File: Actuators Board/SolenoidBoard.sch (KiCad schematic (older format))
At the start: 31 parts, among them J10 Conn_01x02_Male, J9 Conn_01x02_Male, Q1 MMDT2222A

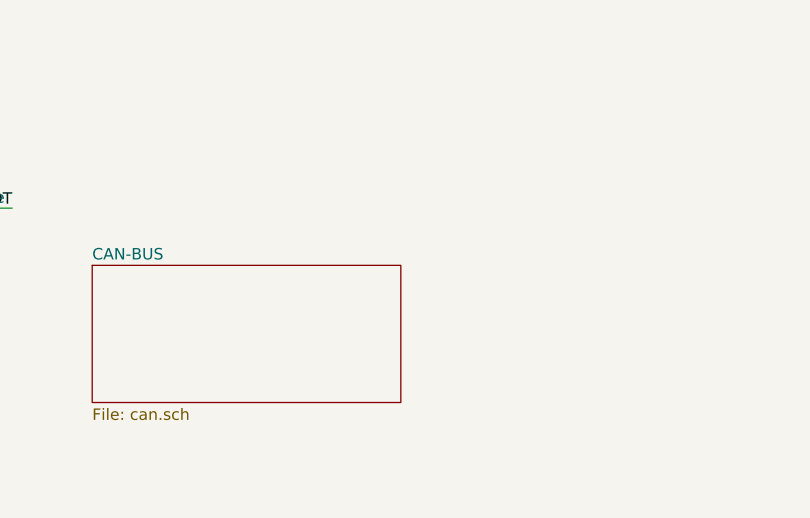
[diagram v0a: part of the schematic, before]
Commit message: Place Hierarchical Pins from CAN sheet to each board.
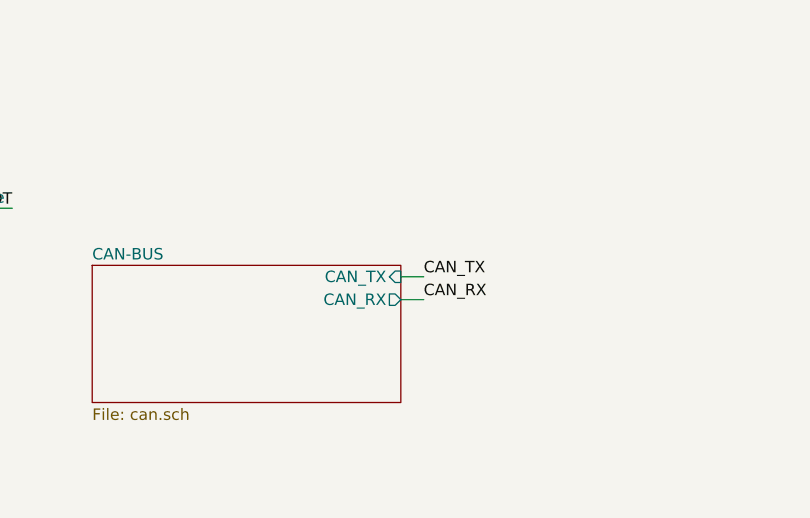
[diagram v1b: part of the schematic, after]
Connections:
- wire segments 78 -> 80
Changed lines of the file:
@@
 F0 "CAN-BUS" 50
 F1 "can.sch" 50
+F2 "CAN_TX" I R 4600 6800 50
+F3 "CAN_RX" O R 4600 6900 50
 $EndSheet
 Text Label 5000 2150 0    50   ~ 0
@@
 Wire Wire Line
 	9600 1350 9750 1350
+Wire Wire Line
+	4600 6800 4700 6800
+Wire Wire Line
+	4600 6900 4700 6900
+Text Label 4700 6800 0    50   ~ 0
+CAN_TX
+Text Label 4700 6900 0    50   ~ 0
+CAN_RX
 $EndSCHEMATC

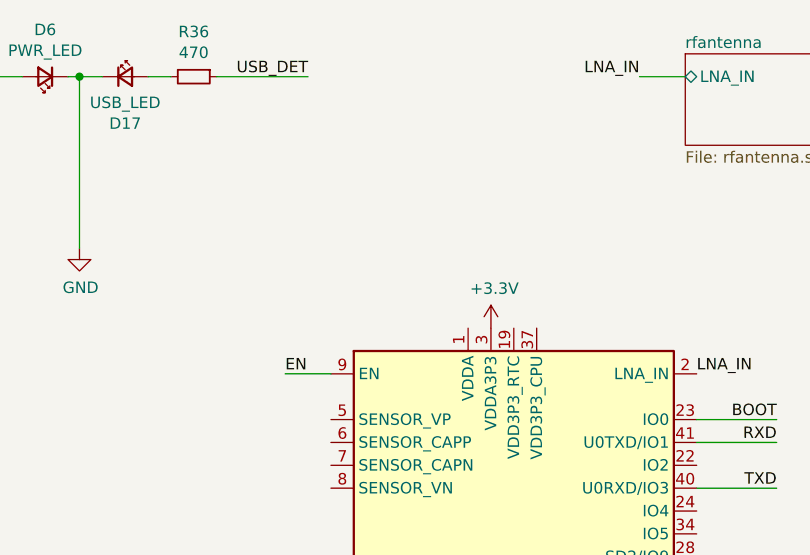
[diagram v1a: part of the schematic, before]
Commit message: Connected 3.3V to ESP32 according to schematic
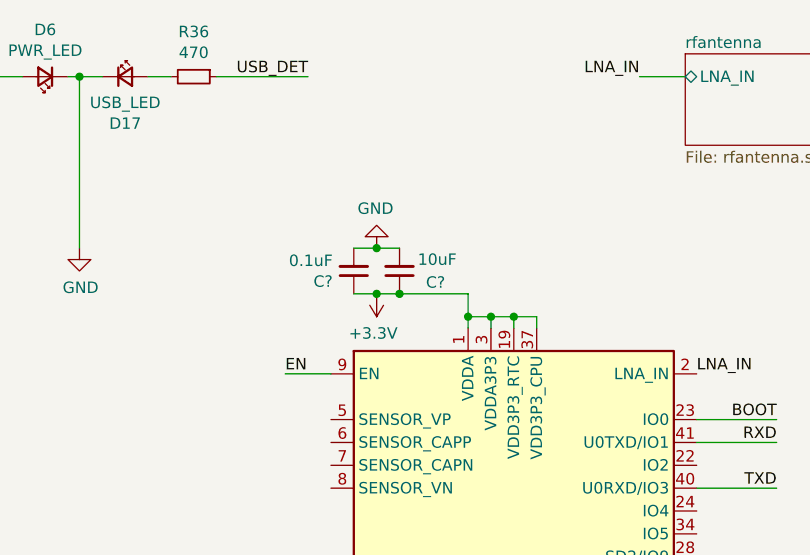
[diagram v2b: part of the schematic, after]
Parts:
- added C?: 10uF, symbol Device:C_Small
- added C?: 0.1uF, symbol Device:C_Small
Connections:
- wire segments 80 -> 93
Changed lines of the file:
@@
 $EndDescr
-$Comp
-L power:+3.3V #PWR020
-U 1 1 5DA60792
-P 4100 1950
-F 0 "#PWR020" H 4100 1800 50  0001 C CNN
-F 1 "+3.3V" H 4115 2123 50  0000 C CNN
-F 2 "" H 4100 1950 50  0001 C CNN
-F 3 "" H 4100 1950 50  0001 C CNN
-	1    4100 1950
-	1    0    0    -1
-$EndComp
 $Comp
 L power:GND #PWR021
@@
 Text Label 4700 6900 0    50   ~ 0
 CAN_RX
+$Comp
+L power:+3.3V #PWR?
+U 1 1 61AA6780
+P 3600 1800
+AR Path="/61AA6780" Ref="#PWR?"  Part="1"
+AR Path="/61AA560B/61AA6780" Ref="#PWR?"  Part="1"
+F 0 "#PWR?" H 3600 1650 50  0001 C CNN
+F 1 "+3.3V" H 3615 1973 50  0000 C CNN
+F 2 "" H 3600 1800 50  0001 C CNN
+F 3 "" H 3600 1800 50  0001 C CNN
+	1    3600 1800
+	-1   0    0    1
+$EndComp
+$Comp
+L Device:C_Small C?
+U 1 1 61AA6786
+P 3700 1700
+AR Path="/61AA6786" Ref="C?"  Part="1"
+AR Path="/61AA560B/61AA6786" Ref="C?"  Part="1"
+F 0 "C?" H 3500 1750 50  0000 L CNN
+F 1 "10uF" H 3450 1650 50  0000 L CNN
+F 2 "" H 3700 1700 50  0001 C CNN
+F 3 "~" H 3700 1700 50  0001 C CNN
+	1    3700 1700
+	-1   0    0    1
+$EndComp
+$Comp
+L Device:C_Small C?
+U 1 1 61AA678C
+P 3500 1700
+AR Path="/61AA678C" Ref="C?"  Part="1"
+AR Path="/61AA560B/61AA678C" Ref="C?"  Part="1"
+F 0 "C?" H 3592 1746 50  0000 L CNN
+F 1 "0.1uF" H 3592 1655 50  0000 L CNN
+F 2 "" H 3500 1700 50  0001 C CNN
+F 3 "~" H 3500 1700 50  0001 C CNN
+	1    3500 1700
+	-1   0    0    1
+$EndComp
+Wire Wire Line
+	3700 1800 3600 1800
+Wire Wire Line
+	3700 1600 3600 1600
+$Comp
+L power:GND #PWR?
+U 1 1 61AA6794
+P 3600 1600
+AR Path="/61AA6794" Ref="#PWR?"  Part="1"
+AR Path="/61AA560B/61AA6794" Ref="#PWR?"  Part="1"
+F 0 "#PWR?" H 3600 1350 50  0001 C CNN
+F 1 "GND" H 3605 1427 50  0000 C CNN
+F 2 "" H 3600 1600 50  0001 C CNN
+F 3 "" H 3600 1600 50  0001 C CNN
+	1    3600 1600
+	-1   0    0    1
+$EndComp
+Connection ~ 3600 1600
+Wire Wire Line
+	3600 1600 3500 1600
+Connection ~ 3600 1800
+Wire Wire Line
+	3600 1800 3500 1800
+Wire Wire Line
+	4000 1900 4100 1900
+Wire Wire Line
+	4100 1900 4100 1950
+Wire Wire Line
+	4000 1900 4000 1950
+Wire Wire Line
+	4100 1900 4200 1900
+Wire Wire Line
+	4200 1900 4200 1950
+Connection ~ 4100 1900
+Wire Wire Line
+	4200 1900 4300 1900
+Wire Wire Line
+	4300 1900 4300 1950
+Connection ~ 4200 1900
+Wire Wire Line
+	3700 1800 4000 1800
+Wire Wire Line
+	4000 1800 4000 1900
+Connection ~ 3700 1800
+Connection ~ 4000 1900
 $EndSCHEMATC

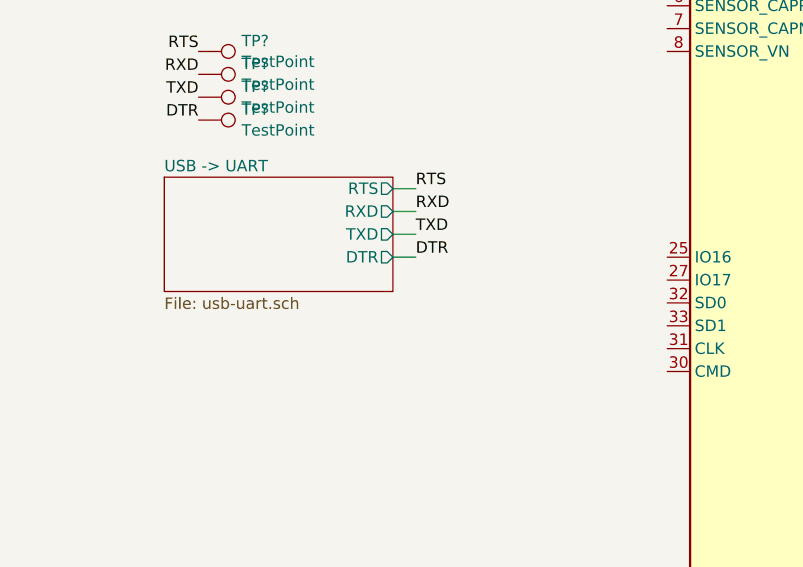
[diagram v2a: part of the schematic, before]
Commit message: Connected 3.3V output from USB-UART converter
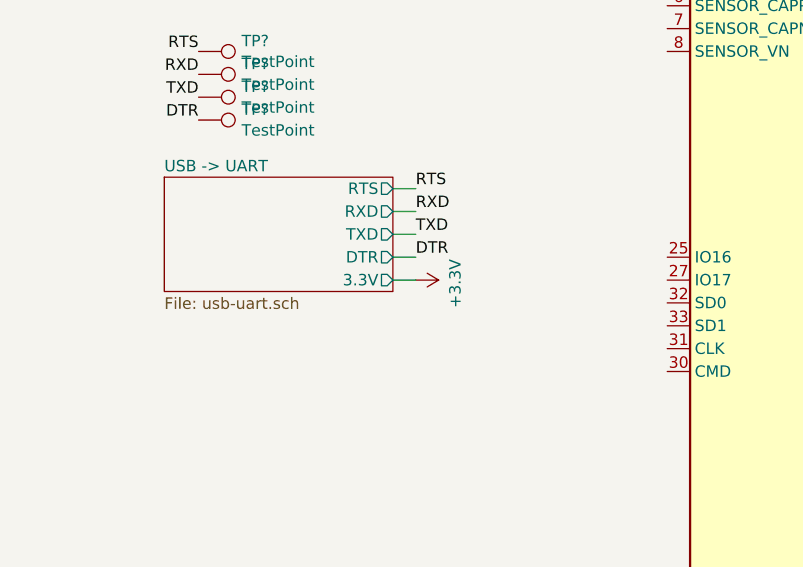
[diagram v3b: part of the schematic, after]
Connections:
- wire segments 93 -> 94
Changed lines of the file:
@@
 F4 "TXD" O R 2200 3450 50
 F5 "DTR" O R 2200 3550 50
+F6 "3.3V" O R 2200 3650 50
 $EndSheet
 $Comp
@@
 Connection ~ 3700 1800
 Connection ~ 4000 1900
+Wire Wire Line
+	2200 3650 2300 3650
+$Comp
+L power:+3.3V #PWR?
+U 1 1 61A6DFD2
+P 2300 3650
+AR Path="/61A6DFD2" Ref="#PWR?"  Part="1"
+AR Path="/61AA560B/61A6DFD2" Ref="#PWR?"  Part="1"
+F 0 "#PWR?" H 2300 3500 50  0001 C CNN
+F 1 "+3.3V" H 2315 3823 50  0000 C CNN
+F 2 "" H 2300 3650 50  0001 C CNN
+F 3 "" H 2300 3650 50  0001 C CNN
+	1    2300 3650
+	0    1    1    0
+$EndComp
 $EndSCHEMATC

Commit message: Swapped IRF620 mosfet with SIJA74DP-T1-GE3
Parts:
- removed Q?: IRF620PBF-BE3, symbol iclr:IRF620PBF-BE3
- added U?: SIJA74DP-T1-GE3, SOT_4DP-T1-GE3_VIS, symbol iclr:SIJA74DP-T1-GE3
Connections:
- wire segments 94 -> 97
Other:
- moved on the sheet: R?
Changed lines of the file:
@@
 LNA_IN
-$Comp
-L iclr:IRF620PBF-BE3 Q?
-U 1 1 61A26E34
-P 9850 2300
-F 0 "Q?" H 9948 2346 50  0000 L CNN
-F 1 "IRF620PBF-BE3" H 9948 2255 50  0000 L CNN
-F 2 "" H 9850 2300 50  0001 C CNN
-F 3 "" H 9850 2300 50  0001 L BNN
-	1    9850 2300
-	1    0    0    -1
-$EndComp
 $Comp
 L Device:D D?
@@
 	1    0    0    -1
 $EndComp
-Text Label 9600 2400 2    50   ~ 0
+Text Label 9450 2450 2    50   ~ 0
 SolEN
 Text Label 5000 3150 0    50   ~ 0
@@
 L power:GND #PWR?
 U 1 1 61A29C79
-P 9850 2650
-F 0 "#PWR?" H 9850 2400 50  0001 C CNN
-F 1 "GND" H 9855 2477 50  0000 C CNN
-F 2 "" H 9850 2650 50  0001 C CNN
-F 3 "" H 9850 2650 50  0001 C CNN
-	1    9850 2650
-	1    0    0    -1
-$EndComp
-Text Label 9850 2100 1    50   ~ 0
+P 9800 2750
+F 0 "#PWR?" H 9800 2500 50  0001 C CNN
+F 1 "GND" H 9805 2577 50  0000 C CNN
+F 2 "" H 9800 2750 50  0001 C CNN
+F 3 "" H 9800 2750 50  0001 C CNN
+	1    9800 2750
+	1    0    0    -1
+$EndComp
+Text Label 9800 2150 1    50   ~ 0
 SolGND
 $Comp
@@
 L Device:R_Small R?
 U 1 1 61A5320F
-P 9600 2550
-F 0 "R?" H 9450 2600 50  0000 L CNN
-F 1 "110" H 9400 2500 50  0000 L CNN
-F 2 "" H 9600 2550 50  0001 C CNN
-F 3 "~" H 9600 2550 50  0001 C CNN
-	1    9600 2550
-	1    0    0    -1
-$EndComp
-Wire Wire Line
-	9600 2450 9600 2400
-Wire Wire Line
-	9600 2400 9650 2400
-Wire Wire Line
-	9600 2650 9850 2650
-Wire Wire Line
-	9850 2650 9850 2500
-Connection ~ 9850 2650
+P 9450 2600
+F 0 "R?" H 9300 2650 50  0000 L CNN
+F 1 "110" H 9250 2550 50  0000 L CNN
+F 2 "" H 9450 2600 50  0001 C CNN
+F 3 "~" H 9450 2600 50  0001 C CNN
+	1    9450 2600
+	1    0    0    -1
+$EndComp
+Wire Wire Line
+	9450 2500 9450 2450
+Wire Wire Line
+	9450 2450 9500 2450
 $Comp
 L Connector:Conn_01x02_Female J?
@@
 	0    1    1    0
 $EndComp
+$Comp
+L iclr:SIJA74DP-T1-GE3 U?
+U 1 1 61AB9D88
+P 9500 2450
+F 0 "U?" H 10100 2550 60  0000 L CNN
+F 1 "SIJA74DP-T1-GE3" H 9962 2447 60  0000 L CNN
+F 2 "SOT_4DP-T1-GE3_VIS" H 9950 2290 60  0001 C CNN
+F 3 "" H 9500 2450 60  0000 C CNN
+	1    9500 2450
+	1    0    0    -1
+$EndComp
+Wire Wire Line
+	9900 2650 9800 2650
+Connection ~ 9800 2650
+Wire Wire Line
+	9800 2650 9700 2650
+Wire Wire Line
+	9450 2700 9450 2750
+Wire Wire Line
+	9450 2750 9800 2750
+Wire Wire Line
+	9800 2750 9800 2650
+Connection ~ 9800 2750
 $EndSCHEMATC

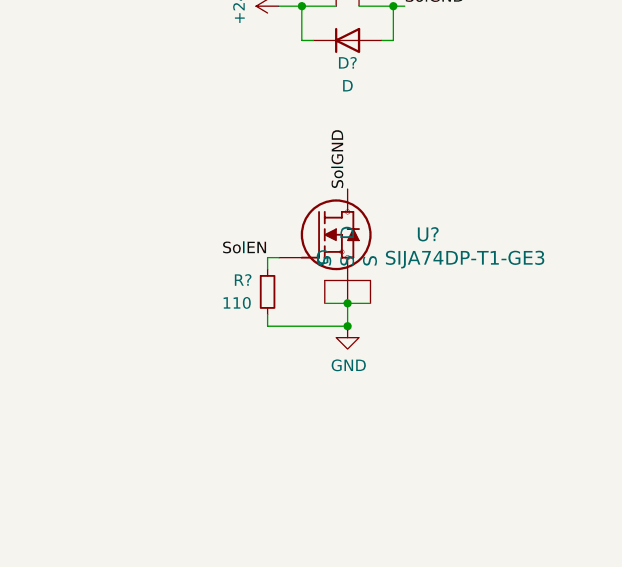
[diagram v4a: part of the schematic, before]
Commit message: Hopefully swapped the mosfet for the last time
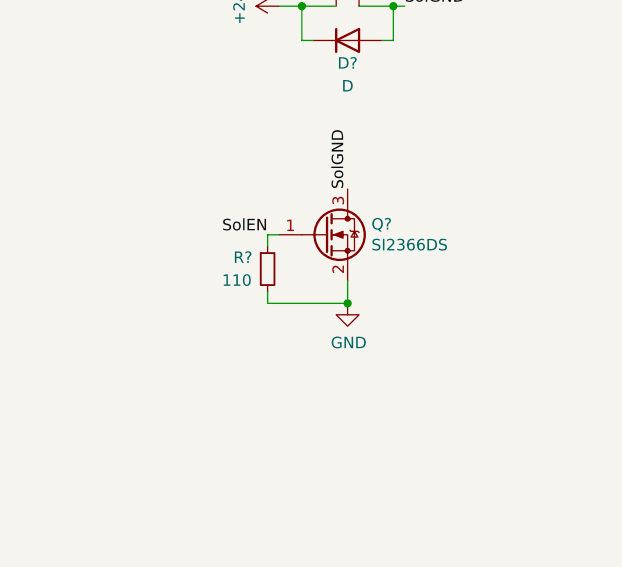
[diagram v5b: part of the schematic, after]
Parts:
- removed U?: SIJA74DP-T1-GE3, SOT_4DP-T1-GE3_VIS, symbol iclr:SIJA74DP-T1-GE3
- added Q?: SI2366DS, Package_TO_SOT_SMD:SOT-23, symbol Transistor_FET:DMN3404L
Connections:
- net GND: now also Q?.2 (S)
- net SolEN: now also Q?.1 (G)
- net SolGND: now also Q?.3 (D)
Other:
- moved on the sheet: R?
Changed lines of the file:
@@
 	1    0    0    -1
 $EndComp
-Text Label 9450 2450 2    50   ~ 0
+Text Label 9450 2350 2    50   ~ 0
 SolEN
 Text Label 5000 3150 0    50   ~ 0
 SolEN
-$Comp
-L power:GND #PWR?
-U 1 1 61A29C79
-P 9800 2750
-F 0 "#PWR?" H 9800 2500 50  0001 C CNN
-F 1 "GND" H 9805 2577 50  0000 C CNN
-F 2 "" H 9800 2750 50  0001 C CNN
-F 3 "" H 9800 2750 50  0001 C CNN
-	1    9800 2750
-	1    0    0    -1
-$EndComp
 Text Label 9800 2150 1    50   ~ 0
 SolGND
@@
 L Device:R_Small R?
 U 1 1 61A5320F
-P 9450 2600
-F 0 "R?" H 9300 2650 50  0000 L CNN
-F 1 "110" H 9250 2550 50  0000 L CNN
-F 2 "" H 9450 2600 50  0001 C CNN
-F 3 "~" H 9450 2600 50  0001 C CNN
-	1    9450 2600
-	1    0    0    -1
-$EndComp
-Wire Wire Line
-	9450 2500 9450 2450
-Wire Wire Line
-	9450 2450 9500 2450
+P 9450 2500
+F 0 "R?" H 9300 2550 50  0000 L CNN
+F 1 "110" H 9250 2450 50  0000 L CNN
+F 2 "" H 9450 2500 50  0001 C CNN
+F 3 "~" H 9450 2500 50  0001 C CNN
+	1    9450 2500
+	1    0    0    -1
+$EndComp
+Wire Wire Line
+	9450 2400 9450 2350
+Wire Wire Line
+	9450 2350 9500 2350
 $Comp
 L Connector:Conn_01x02_Female J?
@@
 	0    1    1    0
 $EndComp
-$Comp
-L iclr:SIJA74DP-T1-GE3 U?
-U 1 1 61AB9D88
-P 9500 2450
-F 0 "U?" H 10100 2550 60  0000 L CNN
-F 1 "SIJA74DP-T1-GE3" H 9962 2447 60  0000 L CNN
-F 2 "SOT_4DP-T1-GE3_VIS" H 9950 2290 60  0001 C CNN
-F 3 "" H 9500 2450 60  0000 C CNN
-	1    9500 2450
-	1    0    0    -1
-$EndComp
-Wire Wire Line
-	9900 2650 9800 2650
+Wire Wire Line
+	9450 2600 9450 2650
+$Comp
+L Transistor_FET:DMN3404L Q?
+U 1 1 61B01102
+P 9700 2350
+F 0 "Q?" H 9904 2396 50  0000 L CNN
+F 1 "SI2366DS" H 9904 2305 50  0000 L CNN
+F 2 "Package_TO_SOT_SMD:SOT-23" H 9900 2275 50  0001 L CIN
+F 3 "http://www.diodes.com/assets/Datasheets/ds31787.pdf" H 9700 2350 50  0001 L CNN
+	1    9700 2350
+	1    0    0    -1
+$EndComp
+Wire Wire Line
+	9800 2550 9800 2650
+Wire Wire Line
+	9800 2650 9450 2650
+$Comp
+L power:GND #PWR?
+U 1 1 61B12B7C
+P 9800 2650
+F 0 "#PWR?" H 9800 2400 50  0001 C CNN
+F 1 "GND" H 9805 2477 50  0000 C CNN
+F 2 "" H 9800 2650 50  0001 C CNN
+F 3 "" H 9800 2650 50  0001 C CNN
+	1    9800 2650
+	1    0    0    -1
+$EndComp
 Connection ~ 9800 2650
-Wire Wire Line
-	9800 2650 9700 2650
-Wire Wire Line
-	9450 2700 9450 2750
-Wire Wire Line
-	9450 2750 9800 2750
-Wire Wire Line
-	9800 2750 9800 2650
-Connection ~ 9800 2750
 $EndSCHEMATC
